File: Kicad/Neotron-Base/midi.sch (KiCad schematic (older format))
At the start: 11 parts, among them J401 DIN-5 180 degree, J402 DIN-5 180 degree, U401 74LS14, U402 6N138

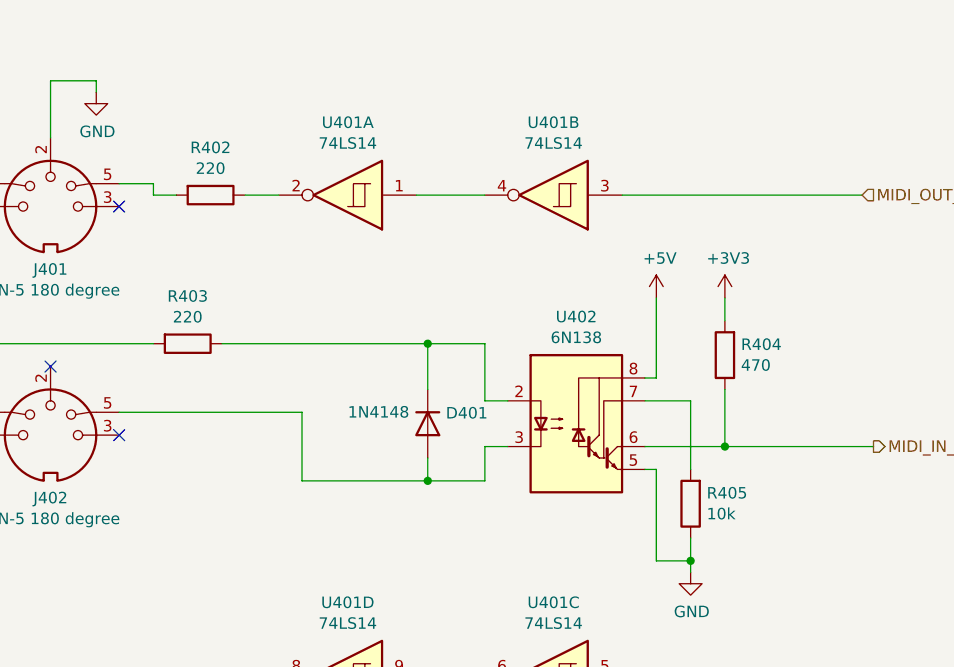
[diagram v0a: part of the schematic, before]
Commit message: Re-work CPU interface to include RMII.
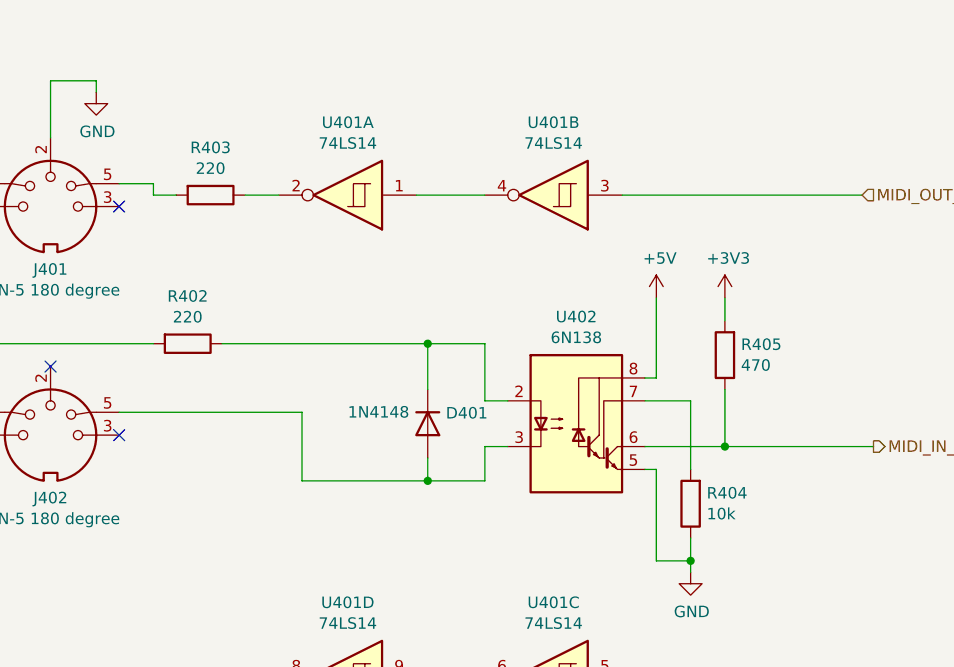
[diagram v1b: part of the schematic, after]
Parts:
- renumbered R403 to R402, R402 to R403, R405 to R404, R404 to R405
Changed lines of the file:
@@
 $Descr A4 11693 8268
 encoding utf-8
-Sheet 4 7
+Sheet 4 10
 Title "Neotron Base"
-Date "2020-08-07"
+Date "2020-08-15"
 Rev "[Uncontrolled]"
 Comp "github.com/neotron-compute"
@@
 $EndComp
 $Comp
-L Device:R R403
+L Device:R R402
 U 1 1 5E03331E
 P 3200 3300
-F 0 "R403" V 2993 3300 50  0000 C CNN
+F 0 "R402" V 2993 3300 50  0000 C CNN
 F 1 "220" V 3084 3300 50  0000 C CNN
 F 2 "Resistor_THT:R_Axial_DIN0207_L6.3mm_D2.5mm_P10.16mm_Horizontal" V 3130 3300 50  0001 C CNN
@@
 $EndComp
 $Comp
-L Device:R R402
+L Device:R R403
 U 1 1 5E0339B9
 P 3300 2650
-F 0 "R402" V 3093 2650 50  0000 C CNN
+F 0 "R403" V 3093 2650 50  0000 C CNN
 F 1 "220" V 3184 2650 50  0000 C CNN
 F 2 "Resistor_THT:R_Axial_DIN0207_L6.3mm_D2.5mm_P10.16mm_Horizontal" V 3230 2650 50  0001 C CNN
@@
 $EndComp
 $Comp
-L Device:R R404
+L Device:R R405
 U 1 1 5E03403F
 P 5550 3350
-F 0 "R404" H 5480 3304 50  0000 R CNN
+F 0 "R405" H 5480 3304 50  0000 R CNN
 F 1 "470" H 5480 3395 50  0000 R CNN
 F 2 "Resistor_THT:R_Axial_DIN0207_L6.3mm_D2.5mm_P10.16mm_Horizontal" V 5480 3350 50  0001 C CNN
@@
 $EndComp
 $Comp
-L Device:R R405
+L Device:R R404
 U 1 1 5E03459E
 P 5400 4000
-F 0 "R405" H 5330 3954 50  0000 R CNN
+F 0 "R404" H 5330 3954 50  0000 R CNN
 F 1 "10k" H 5330 4045 50  0000 R CNN
 F 2 "Resistor_THT:R_Axial_DIN0207_L6.3mm_D2.5mm_P10.16mm_Horizontal" V 5330 4000 50  0001 C CNN
